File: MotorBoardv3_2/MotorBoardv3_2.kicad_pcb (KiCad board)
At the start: 2 copper layers, 128.3 x 158.1 mm, 104 parts, among them J1 Bump0, J11 GP2Y0A41SK0F, J12 GP2Y0A41SK0F, J13 GP2Y0A41SK0F, J15 7.2, J16 LP5.0, J17 ELA, J18 ERA, J19 Voltage Display Port, J2 Bump1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

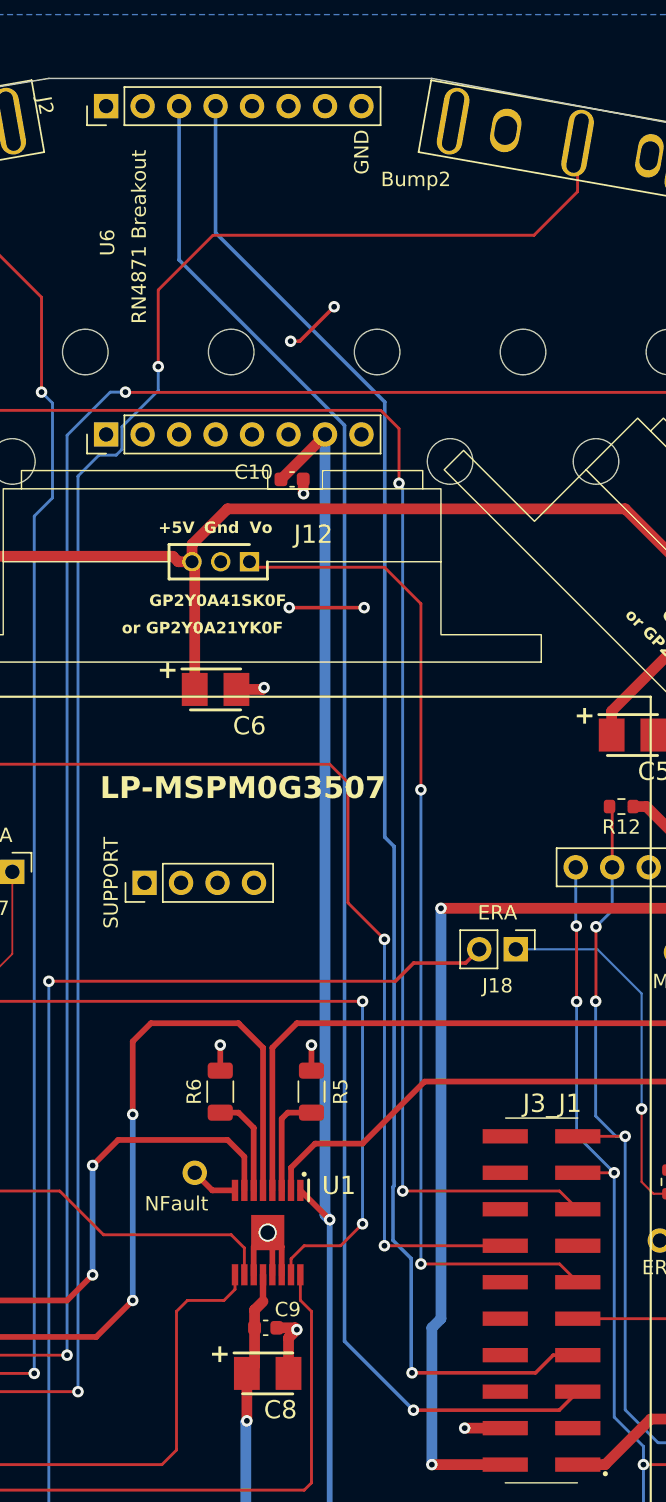
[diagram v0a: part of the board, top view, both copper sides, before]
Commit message: Removed old bluetooth module from schematic and layout
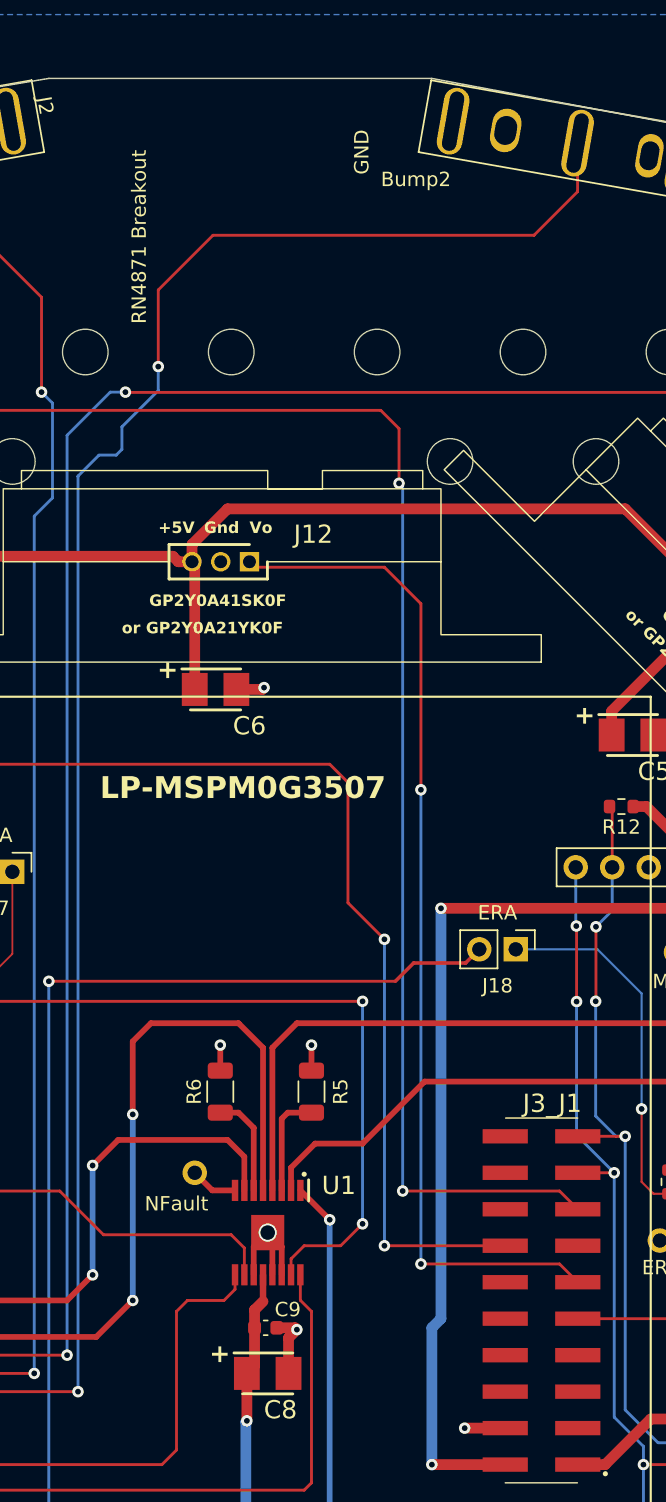
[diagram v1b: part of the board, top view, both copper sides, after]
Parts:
- removed C10: 10uF, RSLK2:C_0603_1608Metric
- removed SUPPORT: PinHeader_1x04_P2.54mm_Vertical, Connector_PinHeader_2.54mm:PinHeader_1x04_P2.54mm_Vertical
- removed U6: RN4871, VoltageDisplay:RN4871_eval
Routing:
- net PA9: track 110.8 -> 1.25 mm, vias 1 -> 0
- net PA8: track 106.0 -> 0.00 mm, vias 1 -> 0
- net +3V3: track 323.7 -> 264.5 mm
- net GND: track 113.1 -> 102.8 mm, vias 19 -> 14

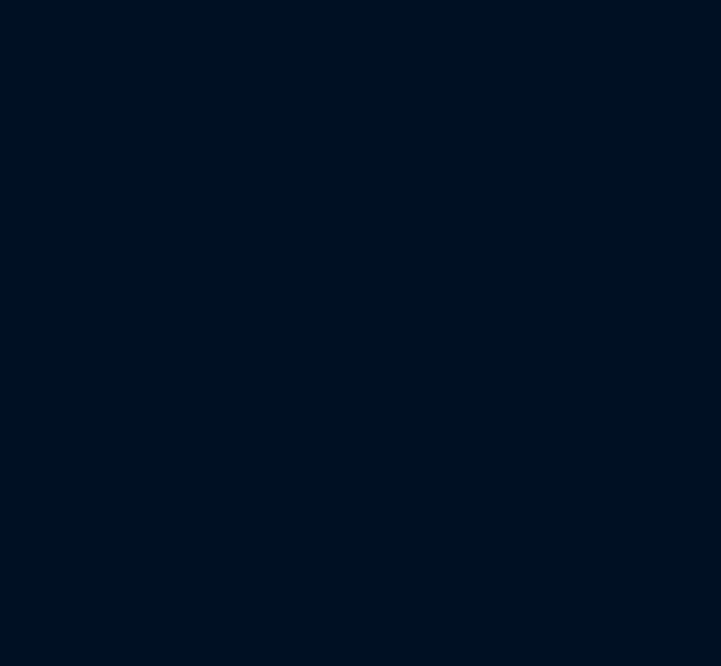
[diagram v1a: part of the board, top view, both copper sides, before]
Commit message: added a possible footprint for button
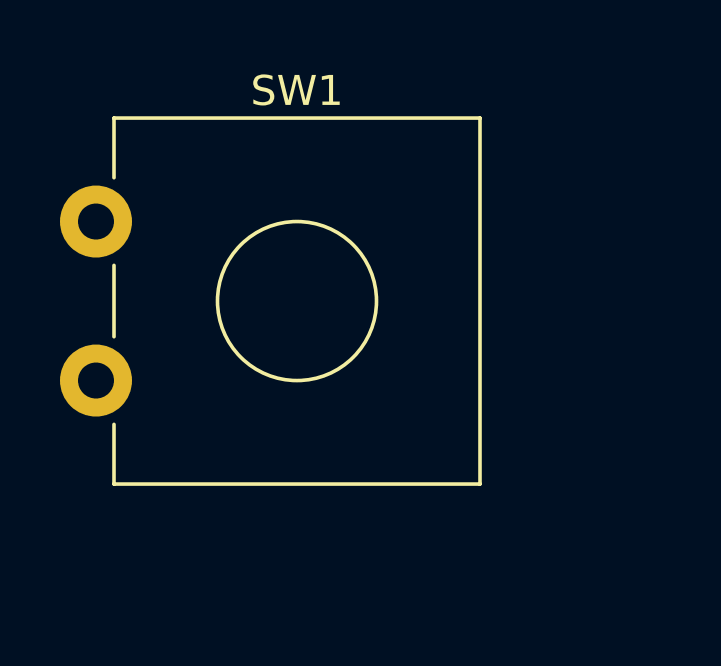
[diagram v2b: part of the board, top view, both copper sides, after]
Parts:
- added SW1: SW_Push, Button_Switch_THT:SW_CW_GPTS203211B, F.Cu at (1.48, 3.62)
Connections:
- J19 pad 1: +7.2V -> Net-(J19-Pin_1)

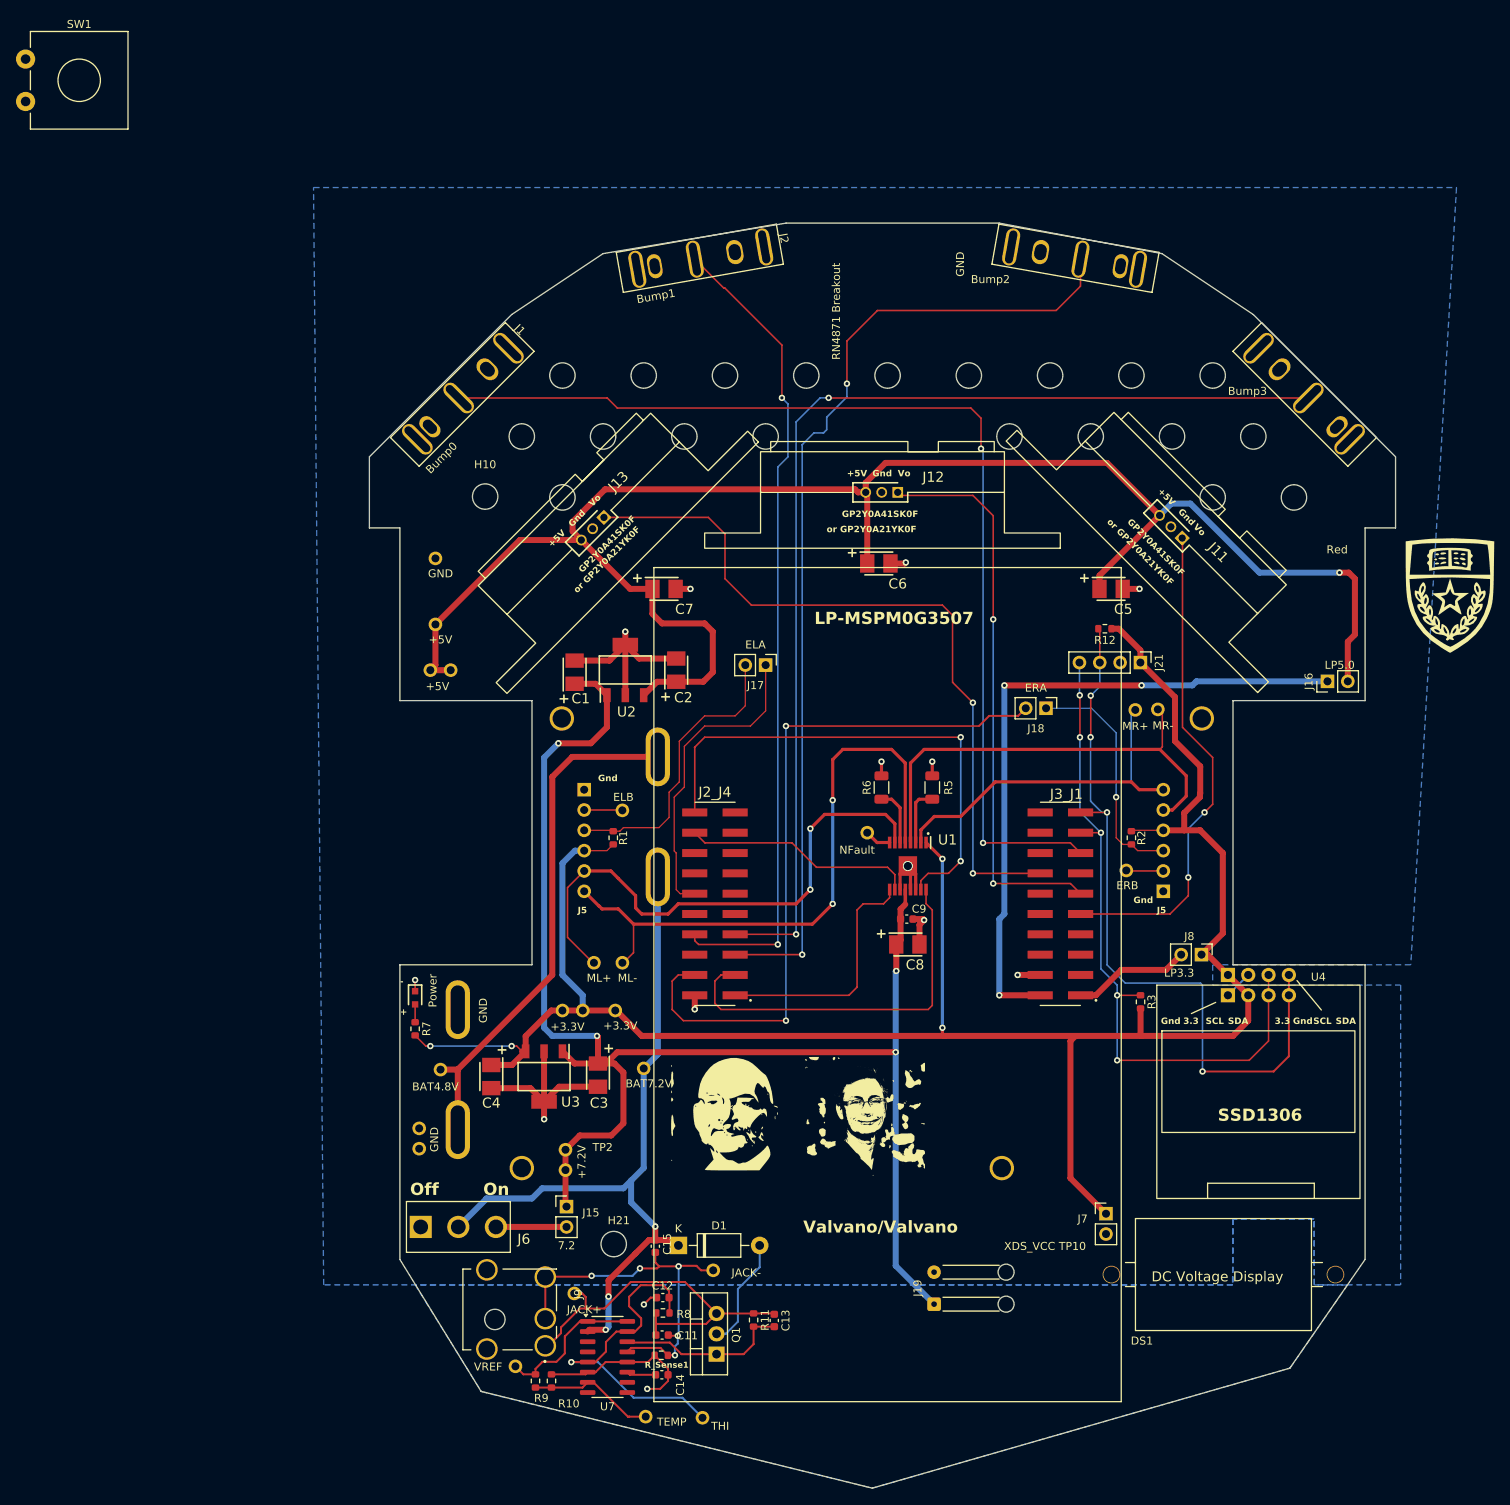
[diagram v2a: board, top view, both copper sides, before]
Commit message: added button for DC Display
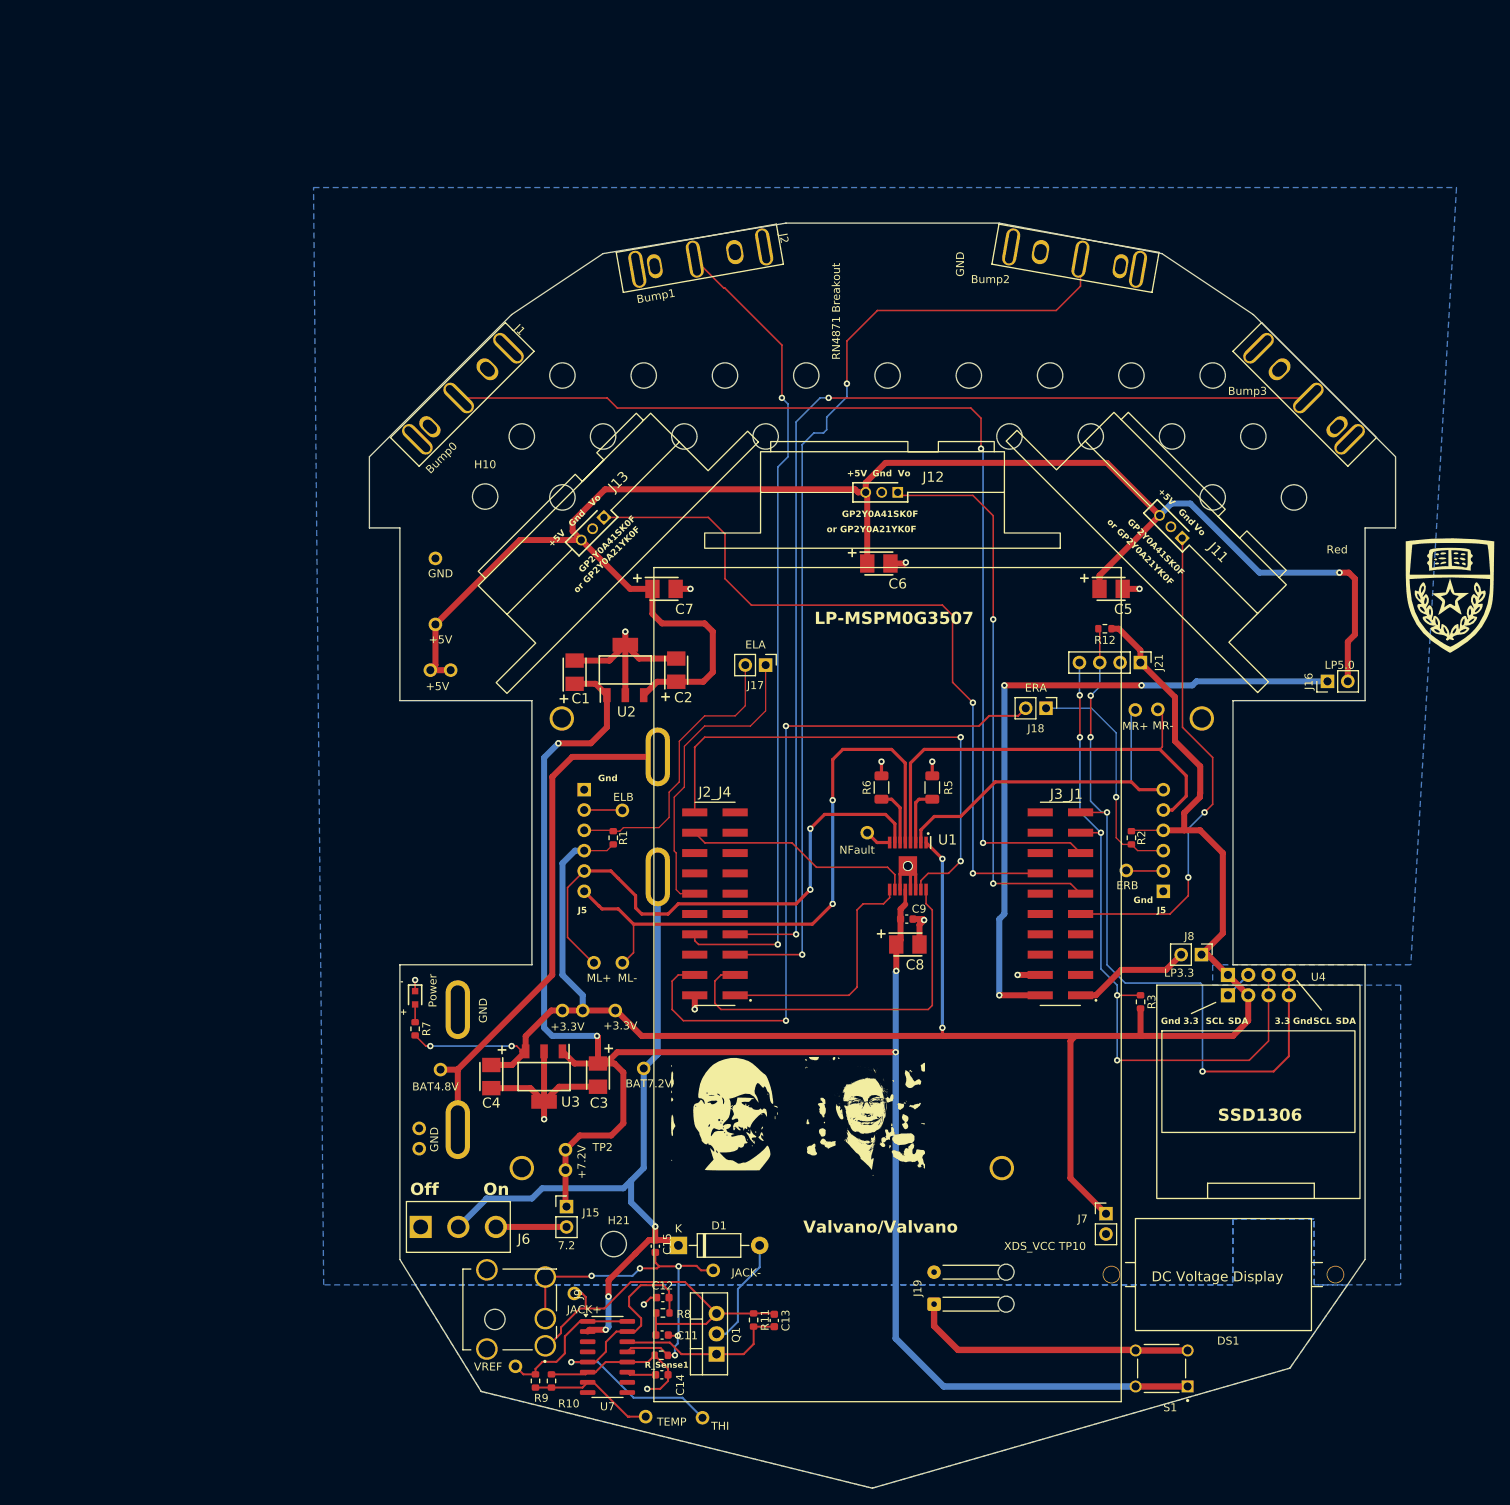
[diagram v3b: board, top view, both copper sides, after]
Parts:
- removed SW1: SW_Push, Button_Switch_THT:SW_CW_GPTS203211B
- added S1: TS02-66-50-BK-160-LCR-D, RSLK2:SW_TS02-66-50-BK-160-LCR-D, F.Cu at (143.5, 167.3)
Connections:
- J19 pad 1: Net-(J19-Pin_1) -> /PushButton_2
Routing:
- net +7.2V: track 185.3 -> 226.6 mm
- net /PushButton_2: track 0.00 -> 35.7 mm

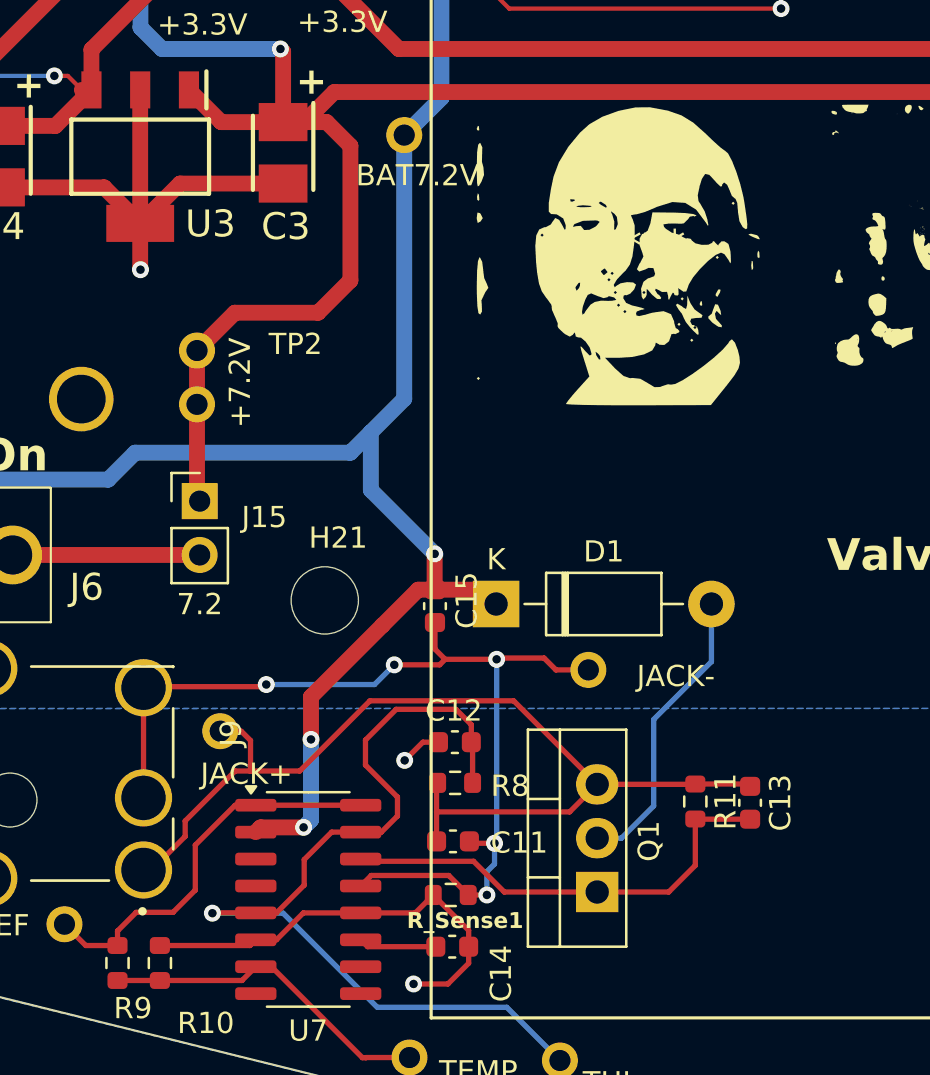
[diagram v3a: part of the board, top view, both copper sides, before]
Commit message: Moved the transistor to not be under the MSPM0G3507
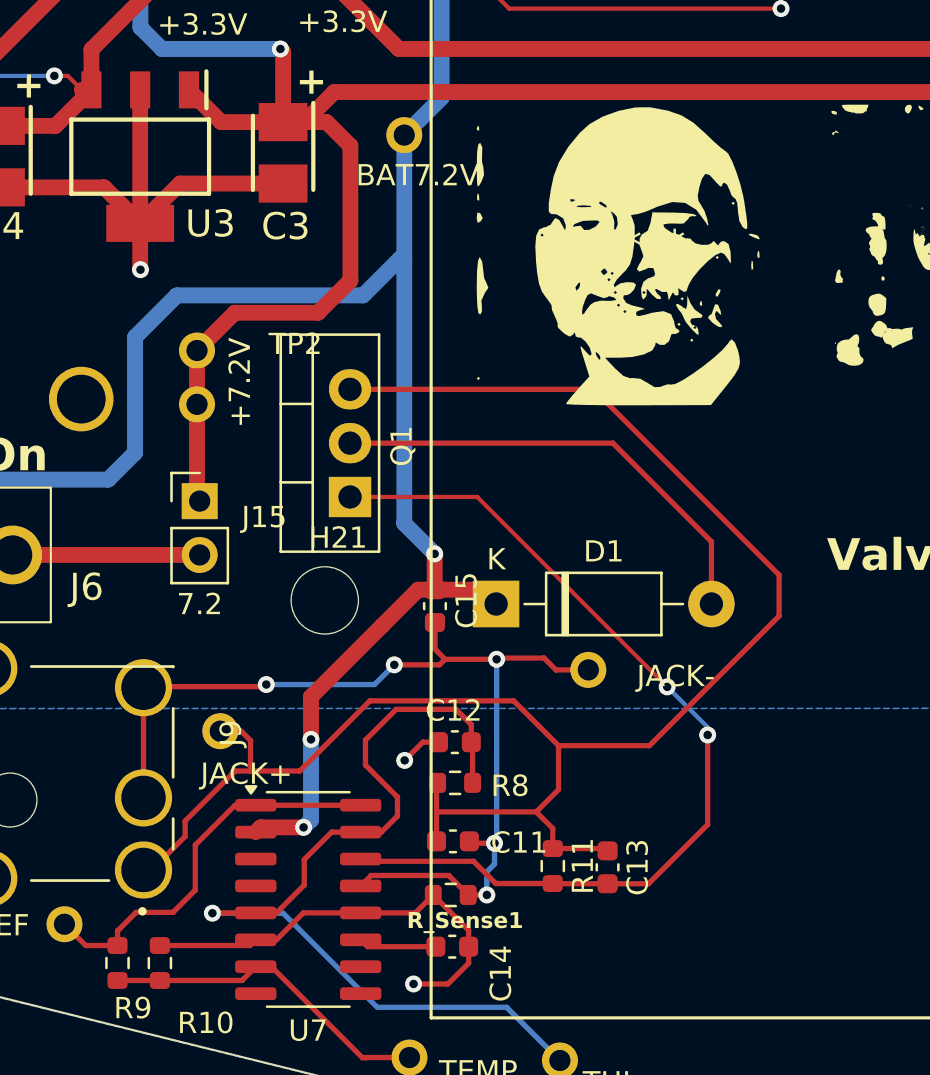
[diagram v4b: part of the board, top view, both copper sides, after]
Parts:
- moved Q1 22.0 mm to (76.2, 146.9)
- moved C13 7.38 mm to (88.3, 164.3)
- moved R11 7.38 mm to (85.7, 164.3)
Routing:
- net Net-(Q1-E): track 47.5 -> 81.3 mm
- net /Charge Circuit/DRV: track 21.7 -> 44.2 mm, vias 0 -> 2
- net Net-(D1-A): track 14.0 -> 21.9 mm
- net BAT7.2V: track 91.9 -> 98.8 mm
